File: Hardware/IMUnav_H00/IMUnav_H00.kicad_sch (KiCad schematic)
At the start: 29 parts, among them J4 Conn_01x03_Pin, SW2 SW_SPST, U7 STM32F446VETx, X1 SX5M24.000M20F30TNN

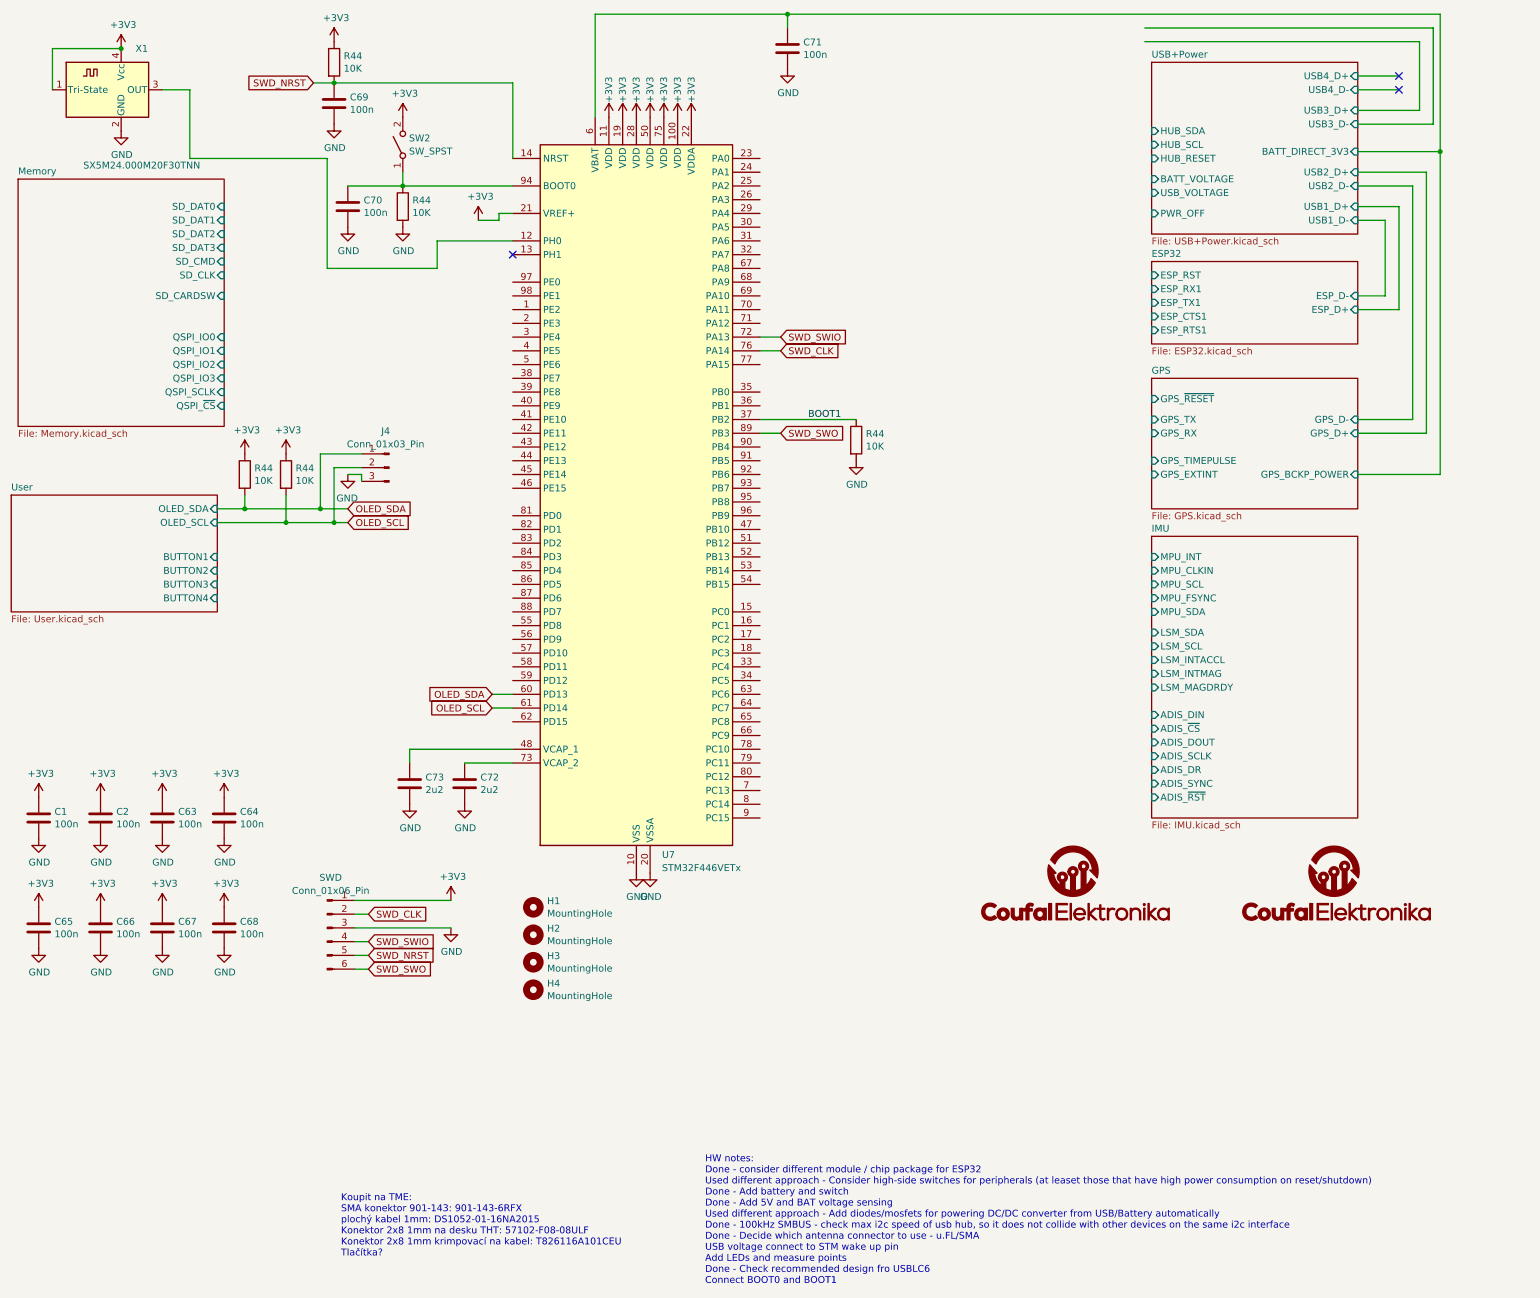
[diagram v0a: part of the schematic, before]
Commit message: Added signal connections to MCU+misc
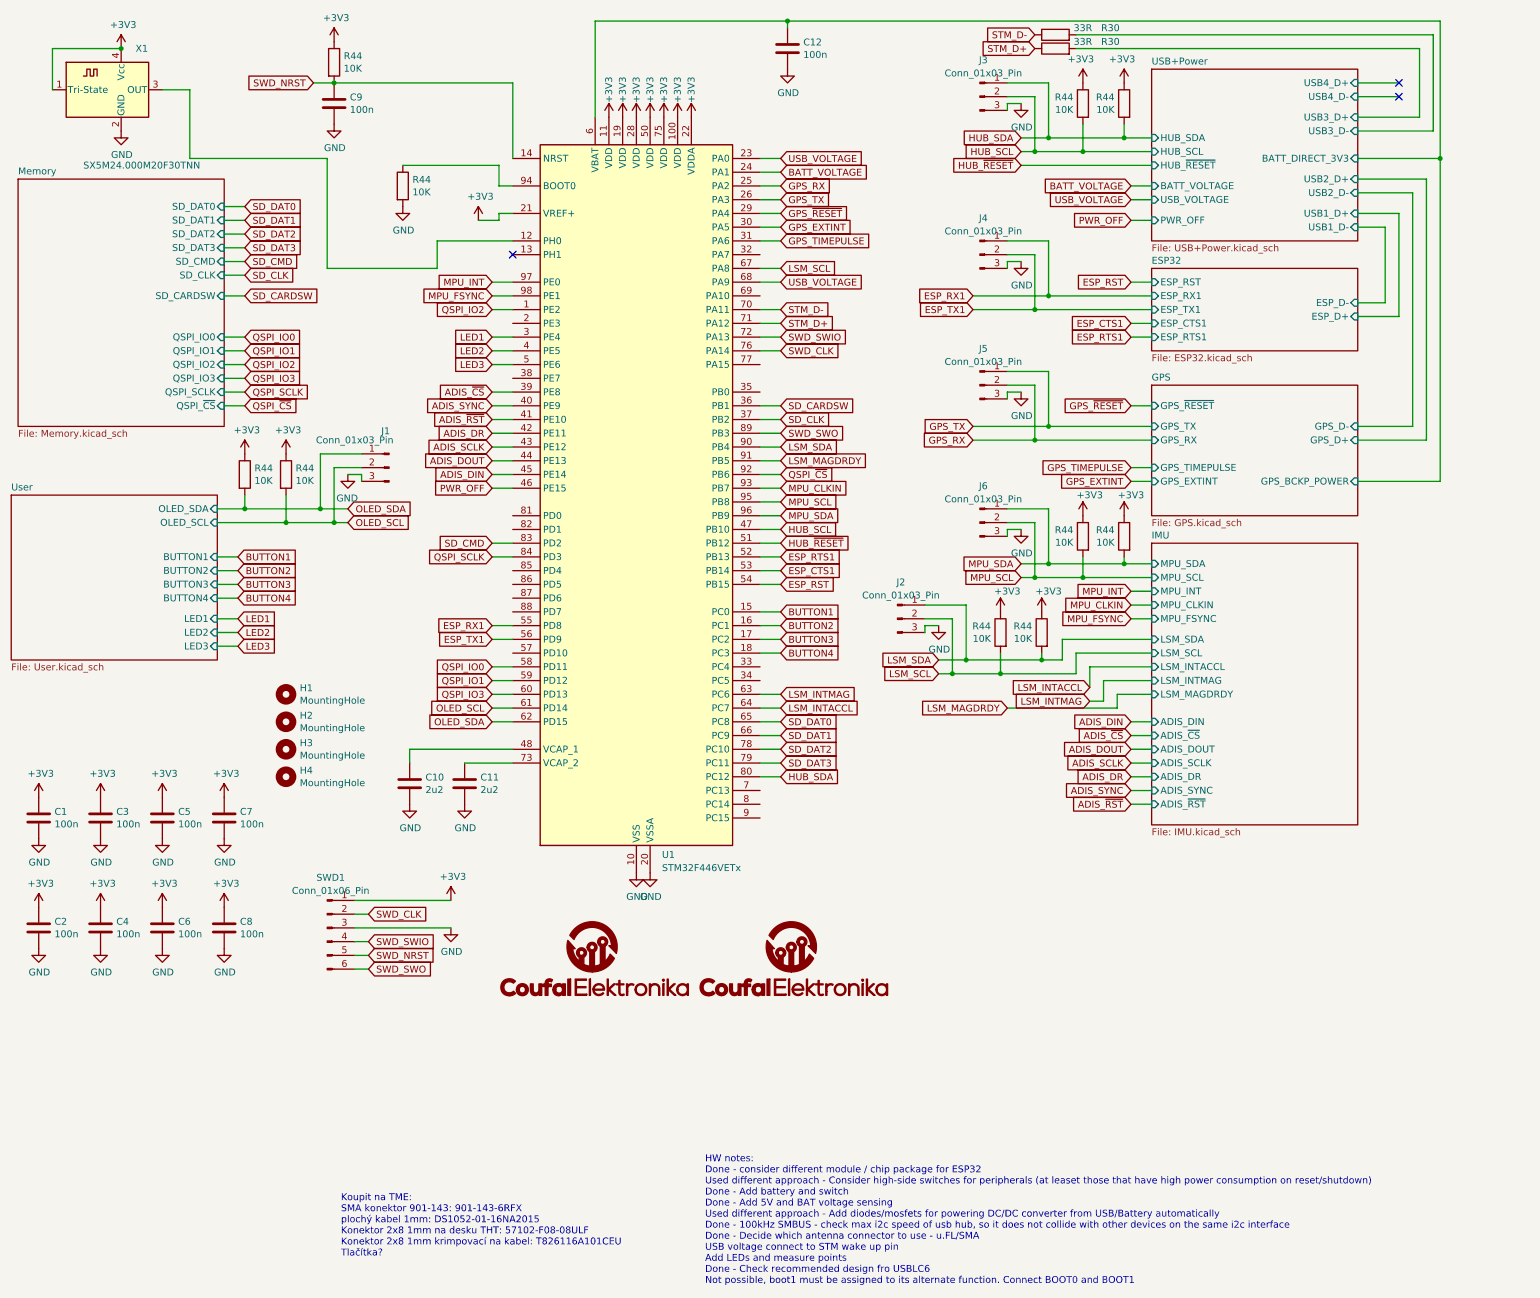
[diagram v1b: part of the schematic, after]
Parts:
- removed C70: 100n, Capacitor_SMD:C_0603_1608Metric, symbol Device:C
- removed R44: 10K, Resistor_SMD:R_0603_1608Metric, symbol Device:R
- removed SW2: SW_SPST, Button_Switch_THT:SW_PUSH_6mm_H13mm, symbol Switch:SW_SPST
- added J2, J3, J4, J5, J6: Conn_01x03_Pin, Connector_PinHeader_2.54mm:PinHeader_1x03_P2.54mm_Vertical, symbol Connector:Conn_01x03_Pin
- added R30 (x2): 33R, Resistor_SMD:R_0603_1608Metric, symbol Device:R
- added R44 (x6): 10K, Resistor_SMD:R_0603_1608Metric, symbol Device:R
- G?: footprint PaLampa_Library:Coufal_elektronika_text_30x13mm -> IMUnav:Coufal_elektronika_text_30x13mm
- G?: footprint PaLampa_Library:Coufal_elektronika_notext_10mm -> IMUnav:Coufal_elektronika_notext_10mm
- J1: renamed from J4; footprint (none) -> Connector_PinHeader_2.54mm:PinHeader_1x03_P2.54mm_Vertical
- renumbered C73 to C10, C72 to C11, C71 to C12, C65 to C2, C2 to C3, C66 to C4, C63 to C5, C67 to C6, C64 to C7, C68 to C8, C69 to C9, SWD to SWD1, U7 to U1
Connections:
- net +3V3: now also R44.1, R44.1, R44.1, R44.1, R44.1, R44.1
- net GND: now also J2.3 (Pin_3), J3.3 (Pin_3), J4.3 (Pin_3), J5.3 (Pin_3), J6.3 (Pin_3)
- net OLED_SDA: now also U1.62 (PD15); no longer U1.60 (PD13)
- net USB+Power/USB3_D+: now also R30.2
- net USB+Power/USB3_D-: now also R30.2
- net QSPI_IO2: now reaches U1.1 (PE2)
- net BUTTON1: now reaches U1.15 (PC0)
- net BUTTON2: now reaches U1.16 (PC1)
- net BUTTON3: now reaches U1.17 (PC2)
- net BUTTON4: now reaches U1.18 (PC3)
- net USB_VOLTAGE: now reaches U1.23 (PA0)
- net USB_VOLTAGE: now also U1.68 (PA9)
- net BATT_VOLTAGE: now reaches U1.24 (PA1)
- net GPS_RX: now reaches U1.25 (PA2)
- net GPS_RX: now also J5.2 (Pin_2)
- net GPS_TX: now reaches U1.26 (PA3)
- net GPS_TX: now also J5.1 (Pin_1)
- net GPS_~{RESET}: now reaches U1.29 (PA4)
- net LED1: now reaches U1.3 (PE4)
- net GPS_EXTINT: now reaches U1.30 (PA5)
- net GPS_TIMEPULSE: now reaches U1.31 (PA6)
- net SD_CARDSW: now reaches U1.36 (PB1)
- net ADIS_~{CS}: now reaches U1.39 (PE8)
- net LED2: now reaches U1.4 (PE5)
- net ADIS_SYNC: now reaches U1.40 (PE9)
- net ADIS_~{RST}: now reaches U1.41 (PE10)
- net ADIS_DR: now reaches U1.42 (PE11)
- net ADIS_SCLK: now reaches U1.43 (PE12)
- net ADIS_DOUT: now reaches U1.44 (PE13)
- net ADIS_DIN: now reaches U1.45 (PE14)
- net PWR_OFF: now reaches U1.46 (PE15)
- net HUB_SCL: now reaches U1.47 (PB10)
- net HUB_SCL: now also J3.2 (Pin_2), R44.2
- net LED3: now reaches U1.5 (PE6)
- net HUB_~{RESET}: now reaches U1.51 (PB12)
- net ESP_RTS1: now reaches U1.52 (PB13)
- net ESP_CTS1: now reaches U1.53 (PB14)
- net ESP_RST: now reaches U1.54 (PB15)
- net ESP_RX1: now reaches U1.55 (PD8)
- net ESP_RX1: now also J4.1 (Pin_1)
- net ESP_TX1: now reaches U1.56 (PD9)
- net ESP_TX1: now also J4.2 (Pin_2)
- net QSPI_IO0: now reaches U1.58 (PD11)
- net QSPI_IO1: now reaches U1.59 (PD12)
- net LSM_INTMAG: now reaches U1.63 (PC6)
- net LSM_INTACCL: now reaches U1.64 (PC7)
- net SD_DAT0: now reaches U1.65 (PC8)
- net SD_DAT1: now reaches U1.66 (PC9)
- net LSM_SCL: now reaches U1.67 (PA8)
- net LSM_SCL: now also J2.2 (Pin_2), R44.2
- net STM_D-: now reaches U1.70 (PA11)
- net STM_D-: now also R30.1
- net STM_D+: now reaches U1.71 (PA12)
- net STM_D+: now also R30.1
- net SD_DAT2: now reaches U1.78 (PC10)
- net SD_DAT3: now reaches U1.79 (PC11)
- net HUB_SDA: now reaches U1.80 (PC12)
- net HUB_SDA: now also J3.1 (Pin_1), R44.2
- net SD_CMD: now reaches U1.83 (PD2)
- net QSPI_SCLK: now reaches U1.84 (PD3)
- net LSM_SDA: now reaches U1.90 (PB4)
- net LSM_SDA: now also J2.1 (Pin_1), R44.2
- net LSM_MAGDRDY: now reaches U1.91 (PB5)
- net QSPI_~{CS}: now reaches U1.92 (PB6)
- net MPU_CLKIN: now reaches U1.93 (PB7)
- net MPU_SCL: now reaches U1.95 (PB8)
- net MPU_SCL: now also J6.2 (Pin_2), R44.2
- net MPU_SDA: now reaches U1.96 (PB9)
- net MPU_SDA: now also J6.1 (Pin_1), R44.2
- net MPU_INT: now reaches U1.97 (PE0)
- net MPU_FSYNC: now reaches U1.98 (PE1)
- net BOOT1 renamed SD_CLK
- new net QSPI_IO3: U1.60 (PD13)
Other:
- sheet USB+Power ports: added HUB_~{RESET}; removed HUB_RESET
- sheet User ports: added LED1, LED2, LED3; removed none
- moved on the sheet: H1, H2, H3, H4, R44

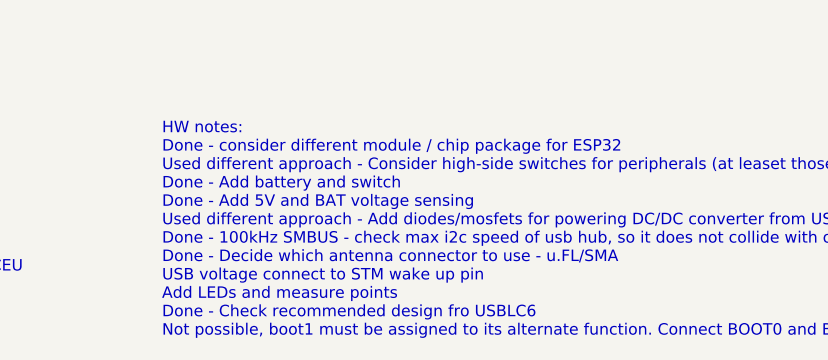
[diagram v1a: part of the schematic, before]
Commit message: Created PCB, configured stackup and DRC
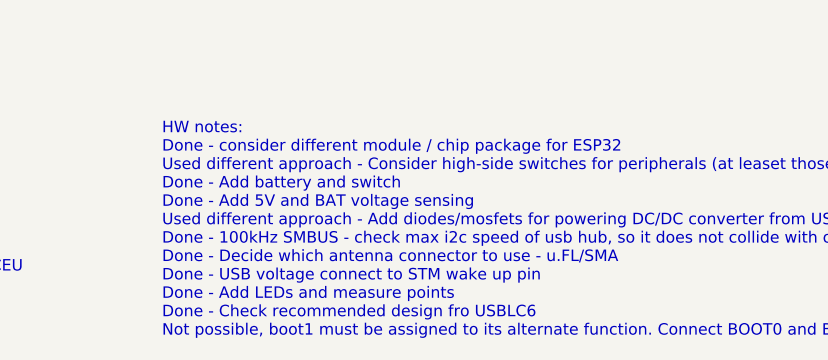
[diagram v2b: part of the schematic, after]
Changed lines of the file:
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@@
     (stroke (width 0) (type default))
   )
-  (text "HW notes:\nDone - consider different module / chip package for ESP32\nUsed different approach - Consider high-side switches for peripherals (at leaset those that have high power consumption on reset/shutdown)\nDone - Add battery and switch\nDone - Add 5V and BAT voltage sensing\nUsed different approach - Add diodes/mosfets for powering DC/DC converter from USB/Battery automatically\nDone - 100kHz SMBUS - check max i2c speed of usb hub, so it does not collide with other devices on the same i2c interface\nDone - Decide which antenna connector to use - u.FL/SMA\nUSB voltage connect to STM wake up pin\nAdd LEDs and measure points\nDone - Check recommended design fro USBLC6\nNot possible, boot1 must be assigned to its alternate function. Connect BOOT0 and BOOT1\n"
+  (text "HW notes:\nDone - consider different module / chip package for ESP32\nUsed different approach - Consider high-side switches for peripherals (at leaset those that have high power consumption on reset/shutdown)\nDone - Add battery and switch\nDone - Add 5V and BAT voltage sensing\nUsed different approach - Add diodes/mosfets for powering DC/DC converter from USB/Battery automatically\nDone - 100kHz SMBUS - check max i2c speed of usb hub, so it does not collide with other devices on the same i2c interface\nDone - Decide which antenna connector to use - u.FL/SMA\nDone - USB voltage connect to STM wake up pin\nDone - Add LEDs and measure points\nDone - Check recommended design fro USBLC6\nNot possible, boot1 must be assigned to its alternate function. Connect BOOT0 and BOOT1\n"
     (at 142.24 247.65 0)
     (effects (font (size 1.27 1.27)) (justify left bottom))
